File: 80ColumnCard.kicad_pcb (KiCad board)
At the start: 2 copper layers, 147.6 x 78.6 mm, 41 parts, among them J1 Apple II Expansion Bus, J2 VIDEO & LIGHT PEN, Q1 2N3904, U1 74LS86, U10 CY7C128, U10B1 CY7C199, U14 74LS157, U15 74LS157, U16 74LS157, U18 74LS273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

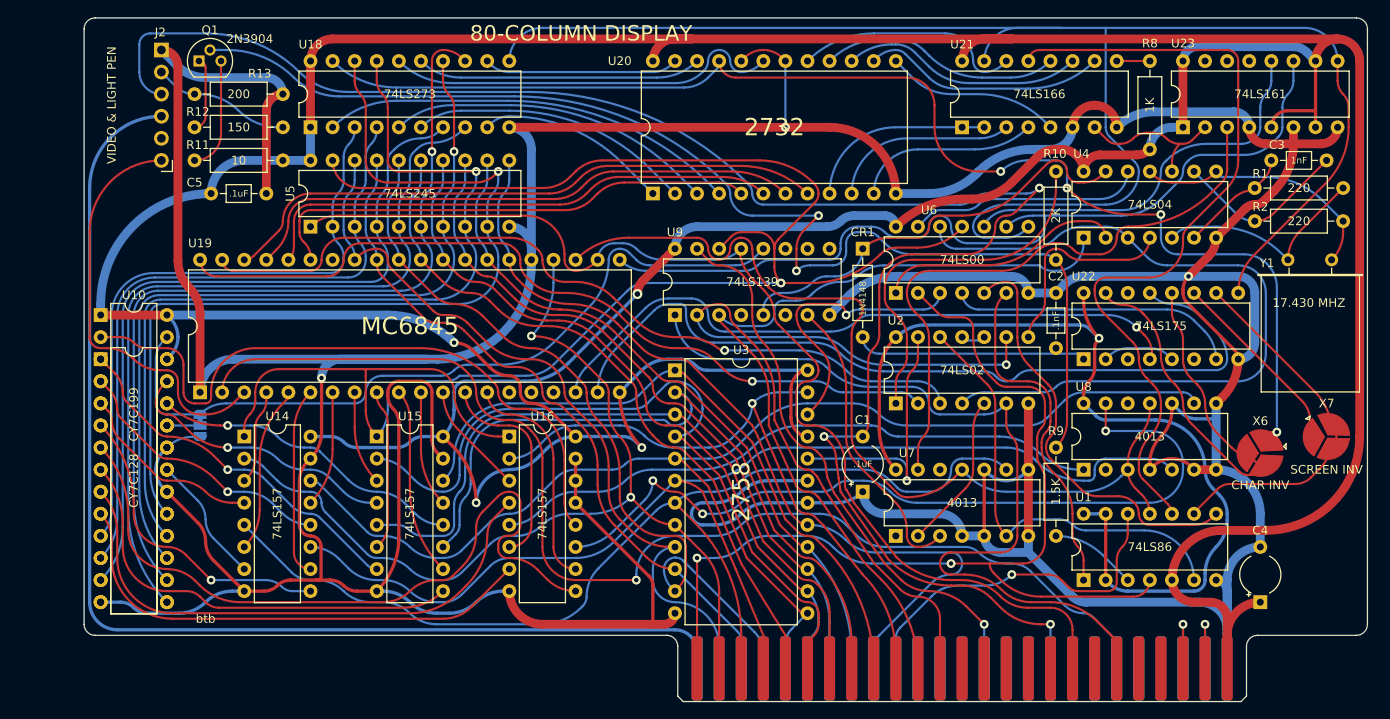
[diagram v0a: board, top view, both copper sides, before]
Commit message: allow bigger RAM and ROM chips
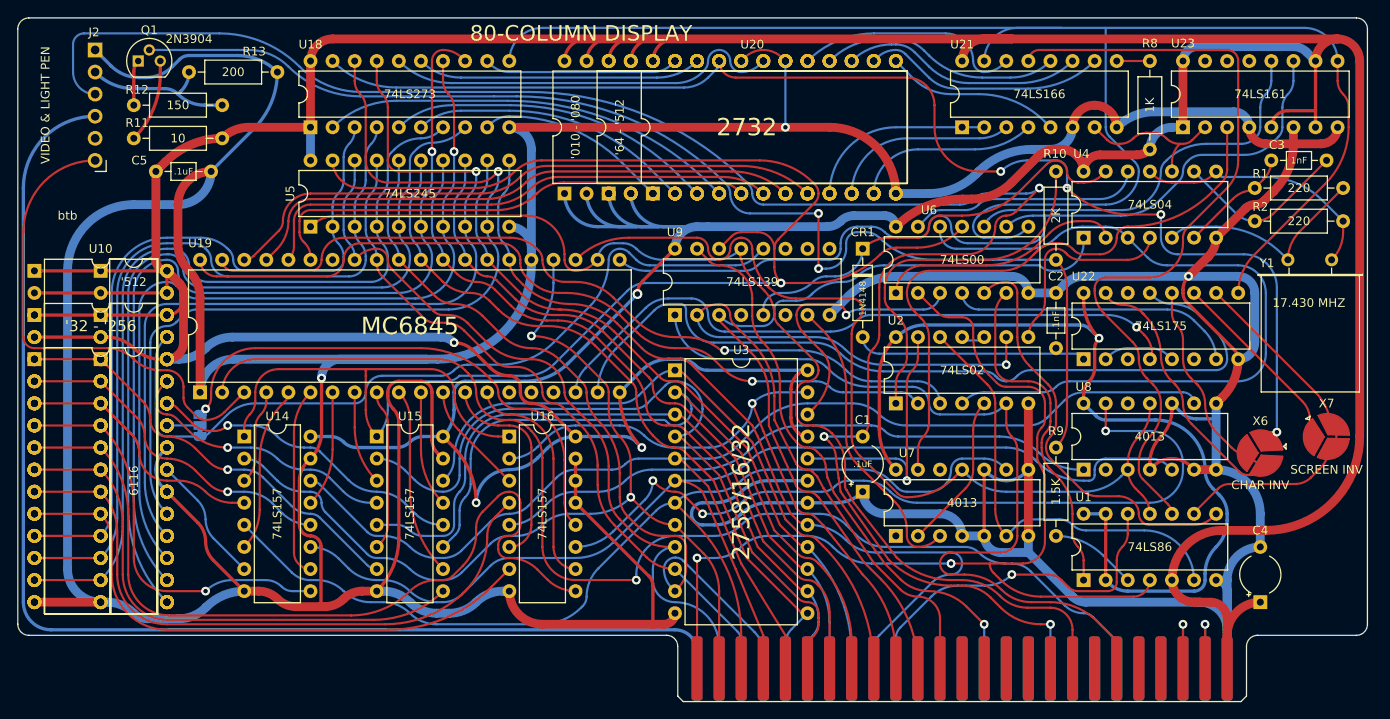
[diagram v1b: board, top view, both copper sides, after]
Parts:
- removed X1: U10: CY7C128* vs CY7C199, Jumper:SolderJumper-3_P1.3mm_Bridged12_RoundedPad1.0x1.5mm_NumberLabels
- added U10N32: '512, Package_DIP:DIP-32_W7.62mm, F.Cu at (102.9, 81.3)
- added U10W24: 6116, MyPackages:DIP-24_W15.24mm, F.Cu at (95.2, 91.4)
- added U10W28: '32 - '256, Package_DIP:DIP-28_W15.24mm, F.Cu at (95.2, 86.4)
- added U10W32: '512, Package_DIP:DIP-32_W15.24mm, F.Cu at (95.2, 81.3)
- added U20B1: '64 - '512, Package_DIP:DIP-28_W15.24mm, F.Cu at (161.3, 72.4)
- added U20C1: '010 - '080, Package_DIP:DIP-32_W15.24mm, F.Cu at (156.2, 72.4)
- added X99: WE/A11, Jumper:SolderJumper-3_P1.3mm_Bridged12_RoundedPad1.0x1.5mm_NumberLabels, B.Cu at (114.3, 99.1)
- U10N24: renamed from U10; value CY7C128 -> 6116
- U10N28: renamed from U10B1; value CY7C199 -> '32 - '256; footprint MyPackages:DIP-28_W7.62mm -> Package_DIP:DIP-28_W7.62mm
- U3: value 2758 -> 2758/16/32
- moved J2 7.62 mm to (102.2, 68.6)
- moved R12 7.43 mm to (106.7, 62.2)
- moved R11 7.43 mm to (116.8, 66.0)
- moved Q1 6.98 mm to (107.2, 57.1)
- moved C5 6.84 mm to (109.2, 69.8)
- moved R13 2.62 mm to (113.0, 58.4)
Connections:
- net /RAMA0 renamed /SRAM/RAMA0
- net /RAMA1 renamed /SRAM/RAMA1
- net /RAMA10 renamed /SRAM/RAMA10
- net /RAMA2 renamed /SRAM/RAMA2
- net /RAMA3 renamed /SRAM/RAMA3
- net /RAMA4 renamed /SRAM/RAMA4
- net /RAMA5 renamed /SRAM/RAMA5
- net /RAMA6 renamed /SRAM/RAMA6
- net /RAMA7 renamed /SRAM/RAMA7
- net /RAMA8 renamed /SRAM/RAMA8
- net /RAMA9 renamed /SRAM/RAMA9
- net Net-(U10B1-Pad27) renamed /SRAM/RAM_R/~{W}
- U10N28 pad 2: /RAMA11 -> +5V
- U16 pad 12: /RAMA11 -> /SRAM/RAMA11
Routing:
- net +5V: track 687.5 -> 807.0 mm
- net /RAMA11: track 75.9 -> 0.00 mm
- net GND: track 733.4 -> 798.7 mm
- net /SRAM/RAMA11: track 0.00 -> 60.0 mm, vias 0 -> 1
- net /SRAM/RAMA0: track 21.6 -> 36.8 mm
- net /E2: track 84.2 -> 97.1 mm
- net /E1: track 75.8 -> 88.6 mm
- net /E0: track 71.2 -> 83.9 mm
- net /SRAM/RAMA10: track 83.5 -> 95.7 mm
- net /SRAM/RAMA2: track 35.2 -> 46.8 mm
- net /SRAM/RAMA6: track 50.1 -> 60.7 mm
- net /SRAM/RAMA8: track 63.6 -> 73.3 mm
- net /SRAM/RAMA9: track 57.0 -> 66.1 mm
- net /LIGHT PEN: track 47.9 -> 56.1 mm
- net /SRAM/RAMA3: track 31.0 -> 38.7 mm
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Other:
- board size 147.6 x 78.6 mm -> 155.2 x 78.6 mm
- board text added: "1-2 6116 2-3 6132-61512"
- board text removed: "1-2 CY7C128 2-3 CY7C199"
